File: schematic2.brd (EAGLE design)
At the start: 101.6 x 53.3 mm, 76 parts, among them IC6 DS3231/SO

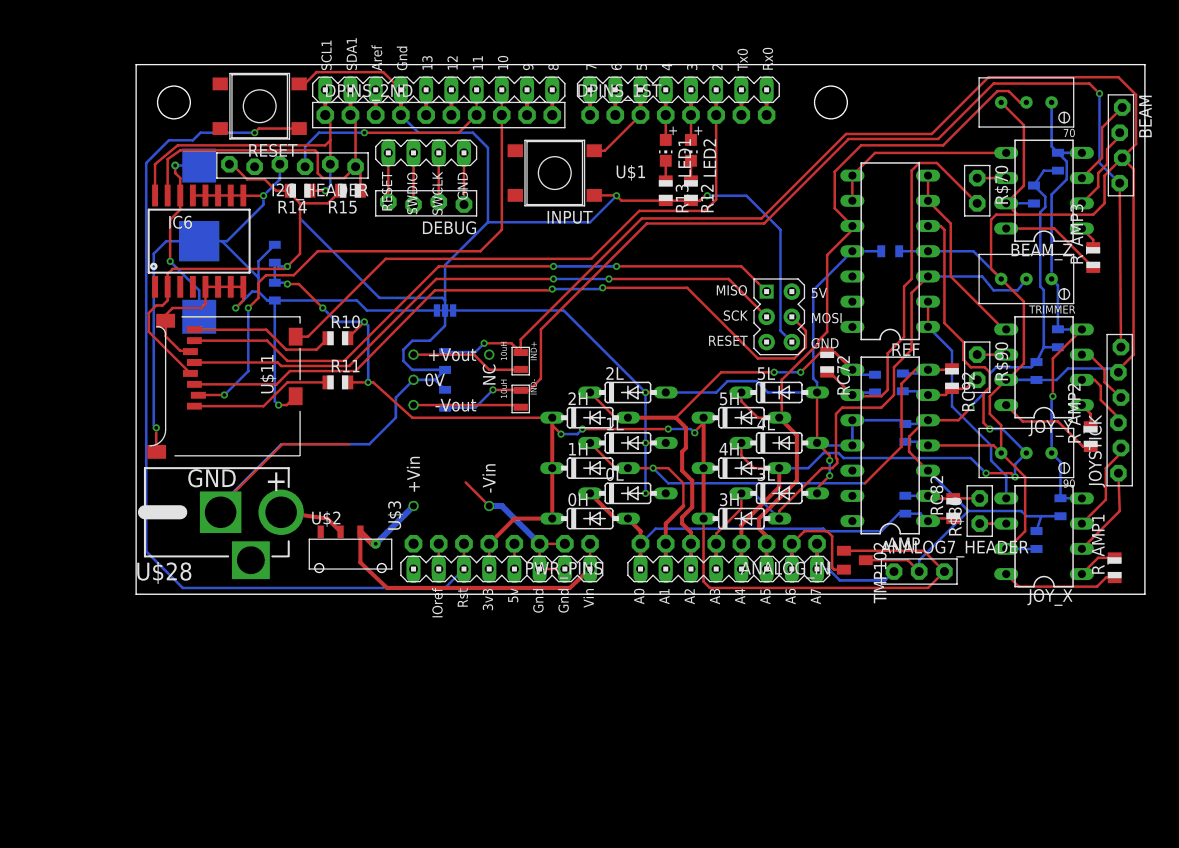
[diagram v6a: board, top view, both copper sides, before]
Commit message: Finished routing top traces, started putting down silkscreen labels. Still need to deal with bottom ground plane.
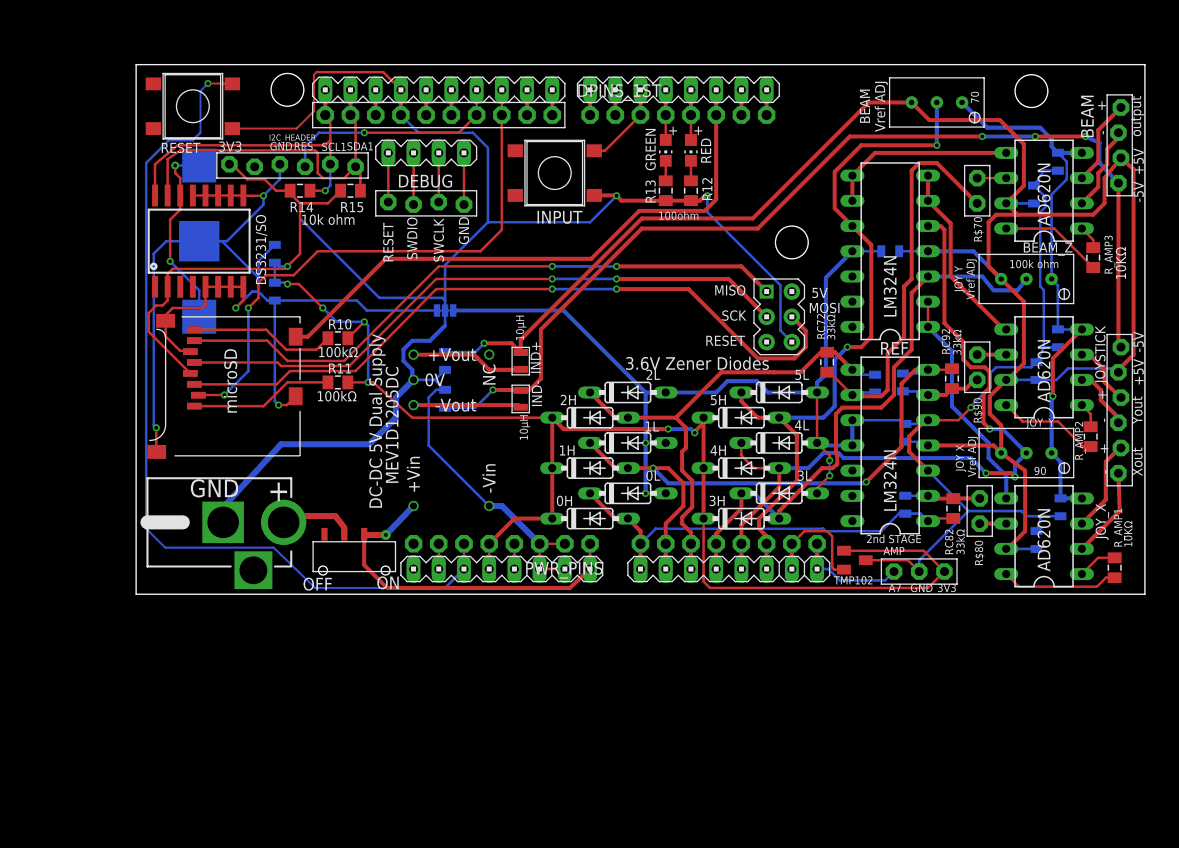
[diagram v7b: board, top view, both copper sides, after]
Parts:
- added STANDOFF3: STAND-OFF, miller:STAND-OFF
- IND+, IND-: value 10uH -> 10µH
- R10, R11: value 100k ohm -> 100kΩ
- RC72, RC82, RC92: value 33k ohm -> 33kΩ
- RESET: value PUSHBUTTON_DPST_SMD -> PUSHBUTTON
- R_AMP1, R_AMP2, R_AMP3: value 10K -> 10KΩ
- moved STANDOFF2 14.6 mm to (66.0, 35.4)
- moved STANDOFF1 11.5 mm to (15.2, 50.8)
- moved 70 9.02 mm to (80.6, 49.5)
- moved U$1 8.89 mm to (0.00, 0.00)
- moved RESET 6.73 mm to (5.71, 49.1)
- moved U$28 1.05 mm to (14.9, 7.24)
- moved U$2 0.46 mm to (22.0, 2.29)
- moved BEAM 0.13 mm to (99.1, 45.2)
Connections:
- net GND: now also RESET.S$1; no longer RESET.P$1
- net RESET: now also RESET.P$1; no longer RESET.S$1
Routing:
- net +5V: track 221.5 -> 198.5 mm
- net -5V: track 109.2 -> 101.7 mm, vias 2 -> 4
- net VNEG: track 50.0 -> 56.9 mm
- net RESET: track 92.8 -> 89.1 mm
- net GND: track 184.6 -> 187.5 mm
- net A5: track 74.9 -> 72.9 mm, vias 0 -> 2
- net VIN: track 38.0 -> 36.3 mm
- net VRAW: track 6.58 -> 7.62 mm
- net AGND: track 174.8 -> 174.5 mm, vias 6 -> 5
- net +3V3: track 180.4 -> 180.3 mm, vias 9 -> 7
- net A1: vias 1 -> 2
- net A2: vias 2 -> 0
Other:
- board text added: "+"
- board text added: "+5V"
- board text added: "-"
- board text added: "-5V"
- board text added: "2nd STAGE AMP"
- board text added: "3.6V Zener Diodes"
- board text added: "3V3"
- board text added: "5V"
- board text added: "A7"
- board text added: "BEAM Vref ADJ"
- board text added: "DC-DC 5V Dual Supply"
- board text added: "GND"
- board text added: "JOY X Vref ADJ"
- board text added: "JOY Y Vref ADJ"
- board text added: "MEV1D1205DC"
- board text added: "MISO"
- board text added: "MOSI"
- board text added: "OFF"
- board text added: "ON"
- board text added: "RES"
- board text added: "RESET"
- board text added: "SCK"
- board text added: "SCL1"
- board text added: "SDA1"
- board text added: "SWCLK"
- board text added: "SWDIO"
- board text added: "TMP102"
- board text added: "Xout"
- board text added: "Yout"
- board text added: "microSD"
- board text added: "output"

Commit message: Added three separate ground pours for DGND, AGND, and GND.
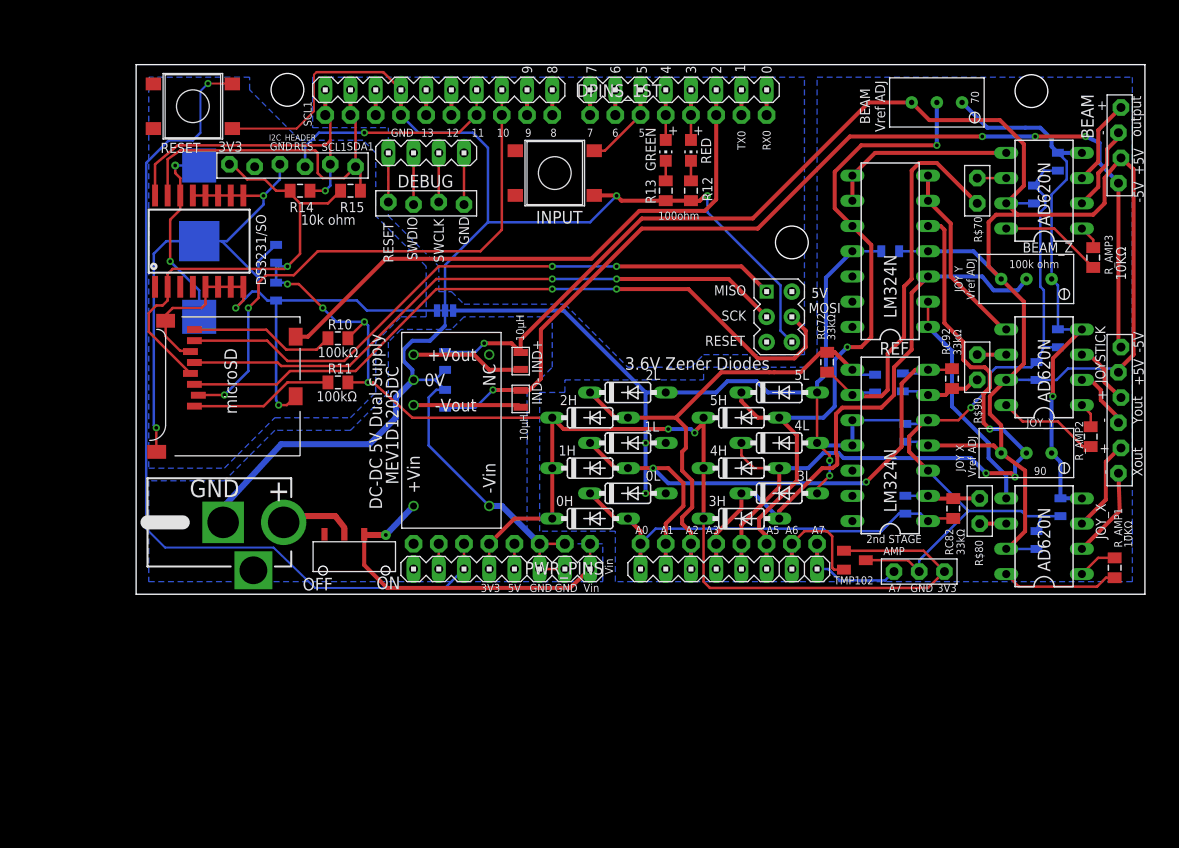
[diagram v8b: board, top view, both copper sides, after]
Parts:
- C15: value 4.7uF -> 4.7µF
- C16, C17, C70, C71, C80, C81, C90, C91: value .1uF -> 0.1µF
- DPINS_2ND: value PINHD-1X10 -> PINHD-1X10CLEAN; device Felicia_force_logger:1X10-BIG -> Felicia_force_logger:1X10-CLEANBIG
- moved C6 0.13 mm to (14.1, 30.5)
- moved C7 0.13 mm to (14.1, 34.3)
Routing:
- net GND: track 187.5 -> 169.5 mm
- added copper zone on layer 16, net AGND
- added copper zone on layer 16, net DGND
- added copper zone on layer 16, net GND
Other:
- board text added: "0"
- board text added: "1"
- board text added: "10"
- board text added: "11"
- board text added: "12"
- board text added: "13"
- board text added: "2"
- board text added: "3"
- board text added: "4"
- board text added: "5"
- board text added: "6"
- board text added: "7"
- board text added: "8"
- board text added: "9"
- board text added: "A0"
- board text added: "A1"
- board text added: "A2"
- board text added: "A3"
- board text added: "A5"
- board text added: "A6"
- board text added: "CR1220"
- board text added: "RX0"
- board text added: "TX0"
- board text added: "Vin"
